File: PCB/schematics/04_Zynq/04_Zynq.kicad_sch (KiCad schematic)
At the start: 0 parts

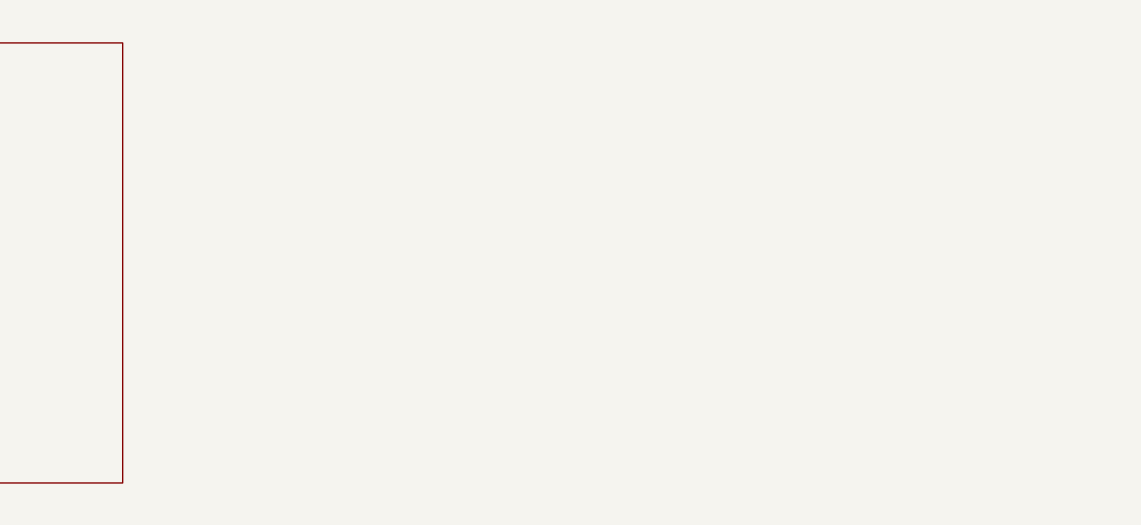
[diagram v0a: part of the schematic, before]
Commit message: Feat: DDR4 Memory added
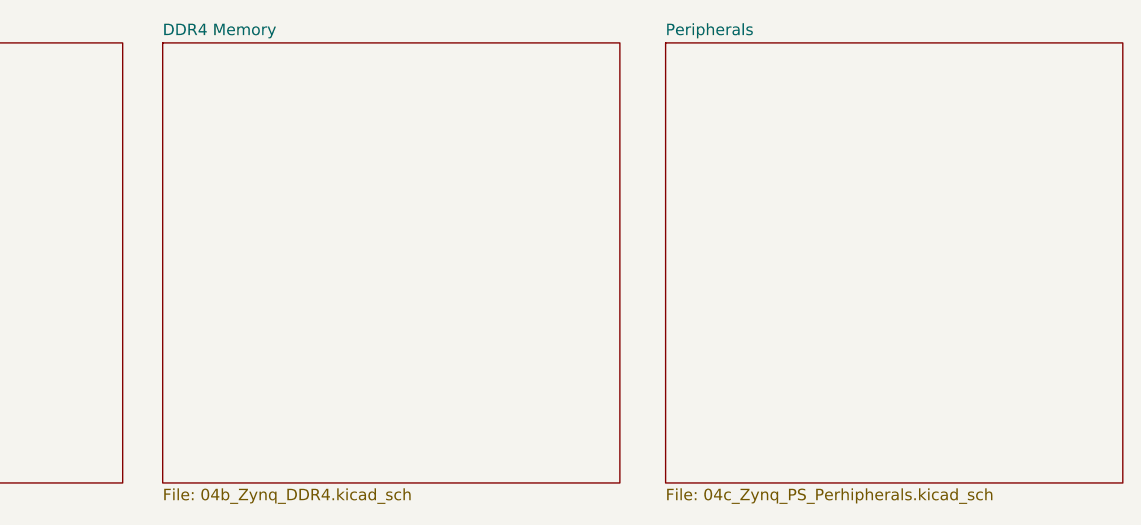
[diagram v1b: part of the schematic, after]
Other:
- added sheet DDR4 Memory (04b_Zynq_DDR4.kicad_sch)
- added sheet Peripherals (04c_Zynq_PS_Perhipherals.kicad_sch)
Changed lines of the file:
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@@
 	(paper "A4")
+	(sheet
+		(at 144.78 33.02)
+		(size 50.8 48.895)
+		(exclude_from_sim no)
+		(in_bom yes)
+		(on_board yes)
+		(dnp no)
+		(fields_autoplaced yes)
+		(stroke
+			(width 0.1524)
+			(type solid)
+		)
+		(fill
+			(color 0 0 0 0)
+		)
+		(property "Sheetname" "Peripherals"
+			(at 144.78 32.3084 0)
+			(show_name no)
+			(do_not_autoplace no)
+			(effects
+				(font
+					(size 1.27 1.27)
+				)
+				(justify left bottom)
+			)
+		)
+		(property "Sheetfile" "04c_Zynq_PS_Perhipherals.kicad_sch"
+			(at 144.78 82.4996 0)
+			(show_name no)
+			(do_not_autoplace no)
+			(effects
+				(font
+					(size 1.27 1.27)
+				)
+				(justify left top)
+			)
+		)
+		(instances
+			(project "Devboard"
+				(path "/f4f7837f-dd80-4f77-b150-4534de1c10d6/b48c92d5-ffe6-40f3-9dff-a09c41a730f7"
+					(page "8")
+				)
+			)
+		)
+	)
+	(sheet
+		(at 88.9 33.02)
+		(size 50.8 48.895)
+		(exclude_from_sim no)
+		(in_bom yes)
+		(on_board yes)
+		(dnp no)
+		(fields_autoplaced yes)
+		(stroke
+			(width 0.1524)
+			(type solid)
+		)
+		(fill
+			(color 0 0 0 0)
+		)
+		(property "Sheetname" "DDR4 Memory"
+			(at 88.9 32.3084 0)
+			(show_name no)
+			(do_not_autoplace no)
+			(effects
+				(font
+					(size 1.27 1.27)
+				)
+				(justify left bottom)
+			)
+		)
+		(property "Sheetfile" "04b_Zynq_DDR4.kicad_sch"
+			(at 88.9 82.4996 0)
+			(show_name no)
+			(do_not_autoplace no)
+			(effects
+				(font
+					(size 1.27 1.27)
+				)
+				(justify left top)
+			)
+		)
+		(instances
+			(project "Devboard"
+				(path "/f4f7837f-dd80-4f77-b150-4534de1c10d6/b48c92d5-ffe6-40f3-9dff-a09c41a730f7"
+					(page "7")
+				)
+			)
+		)
+	)
 	(sheet
 		(at 33.655 33.02)

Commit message: Feat : Completed 04d Peripherals
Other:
- added sheet High Speed Peripherals (04d_Zynq_PS_HighSpeed.kicad_sch)
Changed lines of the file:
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@@
 	(generator "eeschema")
 	(generator_version "10.0")
-	(paper "A4")
+	(paper "User" 841 800)
+	(sheet
+		(at 200.66 33.02)
+		(size 50.8 48.895)
+		(exclude_from_sim no)
+		(in_bom yes)
+		(on_board yes)
+		(dnp no)
+		(fields_autoplaced yes)
+		(stroke
+			(width 0.1524)
+			(type solid)
+		)
+		(fill
+			(color 0 0 0 0)
+		)
+		(property "Sheetname" "High Speed Peripherals"
+			(at 200.66 32.3084 0)
+			(show_name no)
+			(do_not_autoplace no)
+			(effects
+				(font
+					(size 1.27 1.27)
+				)
+				(justify left bottom)
+			)
+		)
+		(property "Sheetfile" "04d_Zynq_PS_HighSpeed.kicad_sch"
+			(at 200.66 82.4996 0)
+			(show_name no)
+			(do_not_autoplace no)
+			(effects
+				(font
+					(size 1.27 1.27)
+				)
+				(justify left top)
+			)
+		)
+		(instances
+			(project "Devboard"
+				(path "/f4f7837f-dd80-4f77-b150-4534de1c10d6/b48c92d5-ffe6-40f3-9dff-a09c41a730f7"
+					(page "9")
+				)
+			)
+		)
+	)
 	(sheet
 		(at 144.78 33.02)

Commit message: feat: Section 4 Done
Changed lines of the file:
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@@
 	(generator "eeschema")
 	(generator_version "10.0")
-	(paper "User" 841 800)
+	(paper "A4")
 	(sheet
-		(at 200.66 33.02)
+		(at 203.2 74.93)
 		(size 50.8 48.895)
 		(exclude_from_sim no)
@@
 		)
 		(property "Sheetname" "High Speed Peripherals"
-			(at 200.66 32.3084 0)
+			(at 203.2 74.2184 0)
 			(show_name no)
 			(do_not_autoplace no)
@@
 		)
 		(property "Sheetfile" "04d_Zynq_PS_HighSpeed.kicad_sch"
-			(at 200.66 82.4996 0)
+			(at 203.2 124.4096 0)
 			(show_name no)
 			(do_not_autoplace no)
@@
 					(page "9")
 				)
+				(path "/f4f7837f-dd80-4f77-b150-4534de1c10d6/54437adb-84e2-431a-8017-9277896bf257"
+					(page "13")
+				)
 			)
 		)
 	)
 	(sheet
-		(at 144.78 33.02)
+		(at 147.32 75.565)
 		(size 50.8 48.895)
 		(exclude_from_sim no)
@@
 		)
 		(property "Sheetname" "Peripherals"
-			(at 144.78 32.3084 0)
+			(at 147.32 74.8534 0)
 			(show_name no)
 			(do_not_autoplace no)
@@
 		)
 		(property "Sheetfile" "04c_Zynq_PS_Perhipherals.kicad_sch"
-			(at 144.78 82.4996 0)
+			(at 147.32 125.0446 0)
 			(show_name no)
 			(do_not_autoplace no)
@@
 					(page "8")
 				)
+				(path "/f4f7837f-dd80-4f77-b150-4534de1c10d6/54437adb-84e2-431a-8017-9277896bf257"
+					(page "12")
+				)
 			)
 		)
 	)
 	(sheet
-		(at 88.9 33.02)
+		(at 91.44 74.93)
 		(size 50.8 48.895)
 		(exclude_from_sim no)
@@
 		)
 		(property "Sheetname" "DDR4 Memory"
-			(at 88.9 32.3084 0)
+			(at 91.44 74.2184 0)
 			(show_name no)
 			(do_not_autoplace no)
@@
 		)
 		(property "Sheetfile" "04b_Zynq_DDR4.kicad_sch"
-			(at 88.9 82.4996 0)
+			(at 91.44 124.4096 0)
 			(show_name no)
 			(do_not_autoplace no)
@@
 					(page "7")
 				)
+				(path "/f4f7837f-dd80-4f77-b150-4534de1c10d6/54437adb-84e2-431a-8017-9277896bf257"
+					(page "14")
+				)
 			)
 		)
 	)
 	(sheet
-		(at 33.655 33.02)
+		(at 36.195 74.93)
 		(size 50.8 48.895)
 		(exclude_from_sim no)
@@
 		)
 		(property "Sheetname" "Zynq CORE"
-			(at 33.655 32.3084 0)
+			(at 36.195 74.2184 0)
 			(show_name no)
 			(do_not_autoplace no)
@@
 		)
 		(property "Sheetfile" "04a_Zynq_Core.kicad_sch"
-			(at 33.655 82.4996 0)
+			(at 36.195 124.4096 0)
 			(show_name no)
 			(do_not_autoplace no)
@@
 					(page "6")
 				)
+				(path "/f4f7837f-dd80-4f77-b150-4534de1c10d6/54437adb-84e2-431a-8017-9277896bf257"
+					(page "11")
+				)
 			)

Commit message: Refactor : Repo
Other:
- note added: "Zynq: Master Page"
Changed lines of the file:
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@@
 		(date "2026-10-31")
+	)
+	(rectangle
+		(start 12.065 12.065)
+		(end 285.115 38.735)
+		(stroke
+			(width 0)
+			(type solid)
+		)
+		(fill
+			(type color)
+			(color 255 229 191 1)
+		)
+	)
+	(text "Zynq: Master Page"
+		(exclude_from_sim no)
+		(at 141.986 30.48 0)
+		(effects
+			(font
+				(face "Montserrat ExtraBold")
+				(size 15 15)
+				(bold yes)
+				(color 0 0 0 1)
+			)
+		)
 	)
 	(sheet
